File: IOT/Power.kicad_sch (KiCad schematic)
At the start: 55 parts, among them J17 24V, J18 12V, J19 5V, J20 3V3, U2 TPS5430DDA, U3 TPS5430DDA, U4 MCP73831-3-OT, U5 MT3608, U6 AMS1117-3.3

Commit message: started pcb
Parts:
- C29: value 47uF/16V -> 47uF/35V; footprint Capacitor_SMD:CP_Elec_6.3x5.4 -> Capacitor_SMD:CP_Elec_8x10
- C30: footprint Capacitor_SMD:CP_Elec_5x5.4 -> Capacitor_SMD:CP_Elec_8x10
- C34: value 22u -> 22u/10V; footprint Capacitor_Tantalum_SMD:CP_EIA-3216-12_Kemet-S_HandSolder -> Capacitor_Tantalum_SMD:CP_EIA-3528-12_Kemet-T_HandSolder
- D13, D7, D8: footprint Diode_SMD:D_SMB-SMC_Universal_Handsoldering -> Diode_SMD:D_SMA_Handsoldering
- L1: value 22uH 2A -> 22uH 3A; footprint Inductor_SMD:L_Wuerth_WE-PD2-Typ-L -> Inductor_SMD:L_Wuerth_WE-PD-Typ-LS_Handsoldering
- L2: footprint Inductor_SMD:L_Wuerth_WE-PD2-Typ-L -> Inductor_SMD:L_Wuerth_WE-PD-Typ-LS_Handsoldering
- L3: footprint Inductor_SMD:L_Wuerth_WE-PD-Typ-M-Typ-S_Handsoldering -> Inductor_SMD:L_Changjiang_FXL0615
- R16: value 4.8k -> 4.7k; footprint Resistor_SMD:R_0805_2012Metric_Pad1.20x1.40mm_HandSolder -> LED_SMD:LED_1206_3216Metric_Pad1.42x1.75mm_HandSolder
- R17, R19, R20, R22, R23, R24, R25, R26, R27: footprint Resistor_SMD:R_0805_2012Metric_Pad1.20x1.40mm_HandSolder -> LED_SMD:LED_1206_3216Metric_Pad1.42x1.75mm_HandSolder
- R18: value 3.8k -> nbt; footprint Resistor_SMD:R_0805_2012Metric_Pad1.20x1.40mm_HandSolder -> LED_SMD:LED_1206_3216Metric_Pad1.42x1.75mm_HandSolder
- R21: value 88.7k -> 120k//330k; footprint Resistor_SMD:R_0805_2012Metric_Pad1.20x1.40mm_HandSolder -> LED_SMD:LED_1206_3216Metric_Pad1.42x1.75mm_HandSolder
- R28: value 420 -> 470; footprint Resistor_SMD:R_0805_2012Metric_Pad1.20x1.40mm_HandSolder -> LED_SMD:LED_1206_3216Metric_Pad1.42x1.75mm_HandSolder
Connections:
- net at D8.1 (K), L2.1: now also C27.2, U3.8 (PH); no longer C27.1, U3.1 (BOOT)
- net Vbat: now reaches BT1.1 (+), C31.1, L3.1, TP10.1, U4.3 (V_{BAT}), U5.4 (EN), U5.5 (IN)
- net at D7.1 (K), L1.1: now also C26.2, U2.8 (PH); no longer C26.1, U2.1 (BOOT)
- new net: C27.1, U3.1 (BOOT)
- new net: C26.1, U2.1 (BOOT)
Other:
- moved on the sheet: C26, C29, C30, D7, D8, L1, L2

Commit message: routed full pcb
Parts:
- added J21: heated blanket, TerminalBlock_Philmore:TerminalBlock_Philmore_TB132_1x02_P5.00mm_Horizontal, symbol Connector:Screw_Terminal_01x02
- added Q1: AO3400A, Package_TO_SOT_SMD:SOT-23, symbol Transistor_FET:AO3400A
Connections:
- net +12V: now also J21.1 (Pin_1)
- net GND: now also Q1.2 (S)
- net VIN: now reaches C24.1, C25.1, J17.1 (Pin_1), R16.1, TP8.1, U2.7 (VIN), U3.7 (VIN)
- new net: J21.2 (Pin_2), Q1.3 (D)
- new net PWMBlanket: Q1.1 (G)
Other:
- moved on the sheet: J18

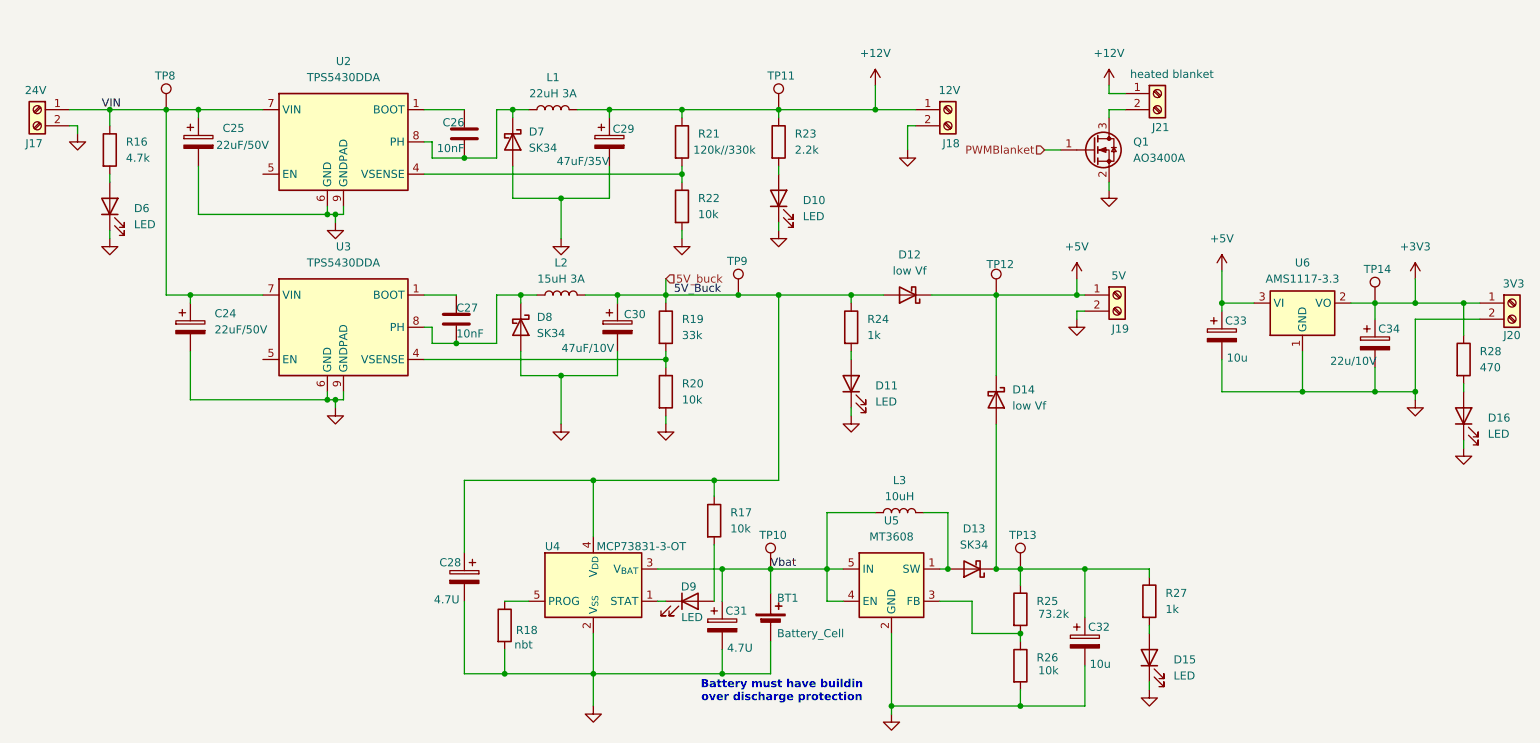
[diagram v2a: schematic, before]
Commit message: added silkscreen and updated footprints
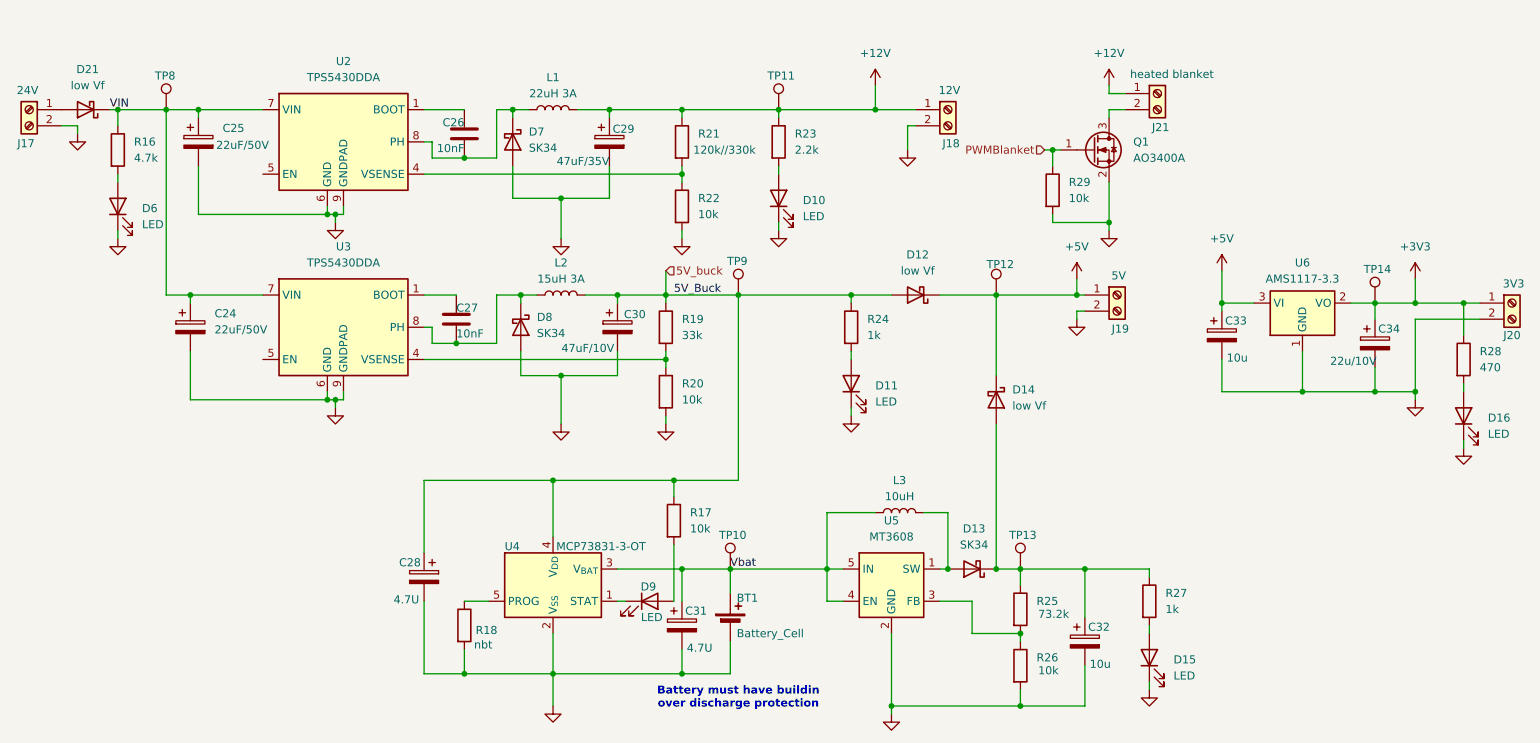
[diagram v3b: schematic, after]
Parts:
- added D21: low Vf, Diode_SMD:D_SMC_Handsoldering, symbol Device:D_Schottky
- added R29: 10k, LED_SMD:LED_1206_3216Metric_Pad1.42x1.75mm_HandSolder, symbol Device:R
- D10, D11, D9: footprint Capacitor_SMD:C_0805_2012Metric_Pad1.18x1.45mm_HandSolder -> Diode_SMD:D_0805_2012Metric_Pad1.15x1.40mm_HandSolder
- D12, D14: footprint Diode_SMD:D_2114_3652Metric_Pad1.85x3.75mm_HandSolder -> Diode_SMD:D_SMC_Handsoldering
- L2: footprint Inductor_SMD:L_Wuerth_WE-PD-Typ-LS_Handsoldering -> Inductor_SMD:L_Bourns_SRP7028A_7.3x6.6mm
- L3: footprint Inductor_SMD:L_Changjiang_FXL0615 -> Inductor_SMD:L_Bourns_SRP7028A_7.3x6.6mm
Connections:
- net GND: now also R29.2
- net PWMBlanket: now also R29.1
- net VIN: now also D21.1 (K); no longer J17.1 (Pin_1)
- new net: D21.2 (A), J17.1 (Pin_1)
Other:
- moved on the sheet: BT1, C28, C31, D12, D6, D9, J17, R16, R17, R18, TP10, U4

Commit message: update PCB and schematic with components we can order
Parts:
- added D22: SK34, Diode_SMD:D_SMA_Handsoldering, symbol Device:D_Schottky
- U5: value MT3608 -> TPS61040DBVR
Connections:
- net +12V: now also D22.1 (K)
- net at J21.2 (Pin_2), Q1.3 (D): now also D22.2 (A)
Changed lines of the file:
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@@
 	)
 	(junction
+		(at 185.42 48.26)
+		(diameter 0)
+		(color 0 0 0 0)
+	)
+	(junction
 		(at 83.82 63.5)
 		(diameter 0)
@@
 	)
 	(junction
+		(at 185.42 55.88)
+		(diameter 0)
+		(color 0 0 0 0)
+	)
+	(junction
 		(at 83.82 144.78)
 		(diameter 0)
@@
 	(wire
 		(pts
+			(xy 182.88 48.26) (xy 185.42 48.26)
+		)
+		(stroke
+			(width 0)
+			(type default)
+		)
+	)
+	(wire
+		(pts
 			(xy 107.95 93.98) (xy 107.95 97.79)
 		)
@@
 	(wire
 		(pts
+			(xy 185.42 48.26) (xy 185.42 53.34)
+		)
+		(stroke
+			(width 0)
+			(type default)
+		)
+	)
+	(wire
+		(pts
 			(xy 233.68 100.33) (xy 233.68 88.9)
 		)
@@
 	(wire
 		(pts
+			(xy 182.88 55.88) (xy 185.42 55.88)
+		)
+		(stroke
+			(width 0)
+			(type default)
+		)
+	)
+	(wire
+		(pts
 			(xy 167.64 85.09) (xy 167.64 97.79)
 		)
@@
 	(wire
 		(pts
-			(xy 185.42 52.07) (xy 185.42 53.34)
+			(xy 185.42 46.99) (xy 185.42 48.26)
 		)
 		(stroke
@@
 	(wire
 		(pts
-			(xy 185.42 55.88) (xy 185.42 57.15)
-		)
-		(stroke
-			(width 0)
-			(type default)
-		)
-	)
-	(wire
-		(pts
 			(xy 92.71 93.98) (xy 92.71 97.79)
 		)
@@
 	(wire
 		(pts
+			(xy 185.42 55.88) (xy 185.42 57.15)
+		)
+		(stroke
+			(width 0)
+			(type default)
+		)
+	)
+	(wire
+		(pts
 			(xy 78.74 90.17) (xy 78.74 92.71)
 		)
@@
 			)
 		)
-		(property "Value" "MT3608"
+		(property "Value" "TPS61040DBVR"
 			(at 151.13 123.19 0)
 			(show_name no)
@@
 	)
 	(symbol
+		(lib_id "Device:D_Schottky")
+		(at 182.88 52.07 90)
+		(mirror x)
+		(unit 1)
+		(body_style 1)
+		(exclude_from_sim no)
+		(in_bom yes)
+		(on_board yes)
+		(in_pos_files yes)
+		(dnp no)
+		(property "Reference" "D22"
+			(at 180.34 50.4824 90)
+			(show_name no)
+			(do_not_autoplace no)
+			(effects
+				(font
+					(size 1.27 1.27)
+				)
+				(justify left)
+			)
+		)
+		(property "Value" "SK34"
+			(at 180.34 53.0224 90)
+			(show_name no)
+			(do_not_autoplace no)
+			(effects
+				(font
+					(size 1.27 1.27)
+				)
+				(justify left)
+			)
+		)
+		(property "Footprint" "Diode_SMD:D_SMA_Handsoldering"
+			(at 182.88 52.07 0)
+			(hide yes)
+			(show_name no)
+			(do_not_autoplace no)
+			(effects
+				(font
+					(size 1.27 1.27)
+				)
+			)
+		)
+		(property "Datasheet" ""
+			(at 182.88 52.07 0)
+			(hide yes)
+			(show_name no)
+			(do_not_autoplace no)
+			(effects
+				(font
+					(size 1.27 1.27)
+				)
+			)
+		)
+		(property "Description" "Schottky diode"
+			(at 182.88 52.07 0)
+			(hide yes)
+			(show_name no)
+			(do_not_autoplace no)
+			(effects
+				(font
+					(size 1.27 1.27)
+				)
+			)
+		)
+		(pin "2"
+		)
+		(pin "1"
+		)
+		(instances
+			(project "IoT"
+				(path "/f5d15b22-d91e-4545-b7af-da23c1769042/f70060c6-2358-4019-84cd-3d9e583a3bdf"
+					(reference "D22")
+					(unit 1)
+				)
+			)
+		)
+	)
+	(symbol
 		(lib_id "Connector:TestPoint")
 		(at 36.83 55.88 0)
@@
 	(symbol
 		(lib_id "power:+12V")
-		(at 185.42 52.07 0)
+		(at 185.42 46.99 0)
 		(unit 1)
 		(body_style 1)
@@
 		(fields_autoplaced yes)
 		(property "Reference" "#PWR066"
-			(at 185.42 55.88 0)
+			(at 185.42 50.8 0)
 			(hide yes)
 			(show_name no)
@@
 		)
 		(property "Value" "+12V"
-			(at 185.42 46.99 0)
+			(at 185.42 41.91 0)
 			(show_name no)
 			(do_not_autoplace no)
@@
 		)
 		(property "Footprint" ""
-			(at 185.42 52.07 0)
+			(at 185.42 46.99 0)
 			(hide yes)
 			(show_name no)
@@
 		)
 		(property "Datasheet" ""
-			(at 185.42 52.07 0)
+			(at 185.42 46.99 0)
 			(hide yes)
 			(show_name no)
@@
 		)
 		(property "Description" "Power symbol creates a global label with name \"+12V\""
-			(at 185.42 52.07 0)
+			(at 185.42 46.99 0)
 			(hide yes)
 			(show_name no)
